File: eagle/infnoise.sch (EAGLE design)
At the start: 25 parts, among them SW1 NS5B1G385DFT2G, SW2 NS5B1G385DFT2G, U1 FT240XQ, X1 USBPCB

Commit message: minor cleanup
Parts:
- renumbered AMP1 to AMP, CMP1 to CMP
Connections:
- net AMP1OUT: now also R9.2; no longer R9.1
- net VCC33: now also R9.1; no longer R9.2
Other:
- moved on the sheet: R9
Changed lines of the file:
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@@
 <part name="R3" library="infnoise" deviceset="RESISTOR" device="0402-RES" value="10K"/>
 <part name="R4" library="infnoise" deviceset="RESISTOR" device="0402-RES" value="10K"/>
-<part name="AMP1" library="infnoise" deviceset="TSV912" device="IQ2T"/>
-<part name="CMP1" library="infnoise" deviceset="TC75W57" device="FK"/>
+<part name="AMP" library="infnoise" deviceset="TSV912" device="IQ2T"/>
+<part name="CMP" library="infnoise" deviceset="TC75W57" device="FK"/>
 <part name="SUPPLY1" library="supply2" deviceset="GND" device=""/>
 <part name="R9" library="infnoise" deviceset="RESISTOR" device="0402-RES" value="8.2K"/>
@@
 <instance part="R3" gate="G$1" x="119.38" y="30.48" rot="R270"/>
 <instance part="R4" gate="G$1" x="119.38" y="10.16" rot="R270"/>
-<instance part="AMP1" gate="G$1" x="208.28" y="50.8"/>
-<instance part="CMP1" gate="G$1" x="208.28" y="15.24"/>
+<instance part="AMP" gate="G$1" x="208.28" y="50.8"/>
+<instance part="CMP" gate="G$1" x="208.28" y="15.24"/>
 <instance part="SUPPLY1" gate="GND" x="66.04" y="-15.24"/>
-<instance part="R9" gate="G$1" x="299.72" y="58.42" rot="R90"/>
+<instance part="R9" gate="G$1" x="299.72" y="58.42" rot="R270"/>
 <instance part="R10" gate="G$1" x="299.72" y="27.94" rot="R90"/>
 <instance part="SW1" gate="G$1" x="142.24" y="50.8"/>
@@
 <wire x1="154.94" y1="35.56" x2="154.94" y2="-10.16" width="0.1524" layer="91"/>
 <wire x1="147.32" y1="40.64" x2="147.32" y2="-10.16" width="0.1524" layer="91"/>
-<pinref part="AMP1" gate="G$1" pin="GND"/>
+<pinref part="AMP" gate="G$1" pin="GND"/>
 <wire x1="182.88" y1="45.72" x2="180.34" y2="45.72" width="0.1524" layer="91"/>
 <wire x1="180.34" y1="45.72" x2="180.34" y2="10.16" width="0.1524" layer="91"/>
-<pinref part="CMP1" gate="G$1" pin="VSS"/>
+<pinref part="CMP" gate="G$1" pin="VSS"/>
 <wire x1="180.34" y1="10.16" x2="180.34" y2="-10.16" width="0.1524" layer="91"/>
 <wire x1="182.88" y1="10.16" x2="180.34" y2="10.16" width="0.1524" layer="91"/>
@@
 <wire x1="147.32" y1="60.96" x2="147.32" y2="88.9" width="0.1524" layer="91"/>
 <wire x1="147.32" y1="88.9" x2="238.76" y2="88.9" width="0.1524" layer="91"/>
-<pinref part="CMP1" gate="G$1" pin="VDD"/>
+<pinref part="CMP" gate="G$1" pin="VDD"/>
 <wire x1="238.76" y1="88.9" x2="276.86" y2="88.9" width="0.1524" layer="91"/>
 <wire x1="276.86" y1="88.9" x2="299.72" y2="88.9" width="0.1524" layer="91"/>
 <wire x1="236.22" y1="25.4" x2="238.76" y2="25.4" width="0.1524" layer="91"/>
 <wire x1="238.76" y1="25.4" x2="238.76" y2="60.96" width="0.1524" layer="91"/>
-<pinref part="AMP1" gate="G$1" pin="VCC"/>
+<pinref part="AMP" gate="G$1" pin="VCC"/>
 <wire x1="238.76" y1="60.96" x2="238.76" y2="88.9" width="0.1524" layer="91"/>
 <wire x1="236.22" y1="60.96" x2="238.76" y2="60.96" width="0.1524" layer="91"/>
-<pinref part="R9" gate="G$1" pin="2"/>
-<wire x1="299.72" y1="63.5" x2="299.72" y2="88.9" width="0.1524" layer="91"/>
 <pinref part="SW1" gate="G$1" pin="VCC"/>
 <pinref part="SW2" gate="G$1" pin="VCC"/>
@@
 <wire x1="119.38" y1="35.56" x2="119.38" y2="88.9" width="0.1524" layer="91"/>
 <junction x="119.38" y="88.9"/>
+<pinref part="R9" gate="G$1" pin="1"/>
+<wire x1="299.72" y1="88.9" x2="299.72" y2="63.5" width="0.1524" layer="91"/>
 </segment>
 </net>
 <net name="A" class="0">
 <segment>
-<pinref part="AMP1" gate="G$1" pin="IN1+"/>
+<pinref part="AMP" gate="G$1" pin="IN1+"/>
 <wire x1="182.88" y1="50.8" x2="162.56" y2="50.8" width="0.1524" layer="91"/>
 <pinref part="C7" gate="G$1" pin="1"/>
@@
 <wire x1="154.94" y1="50.8" x2="149.86" y2="50.8" width="0.1524" layer="91"/>
 <wire x1="154.94" y1="43.18" x2="154.94" y2="50.8" width="0.1524" layer="91"/>
-<pinref part="CMP1" gate="G$1" pin="IN1+"/>
+<pinref part="CMP" gate="G$1" pin="IN1+"/>
 <wire x1="182.88" y1="15.24" x2="162.56" y2="15.24" width="0.1524" layer="91"/>
 <wire x1="162.56" y1="15.24" x2="162.56" y2="50.8" width="0.1524" layer="91"/>
@@
 <wire x1="180.34" y1="76.2" x2="292.1" y2="76.2" width="0.1524" layer="91"/>
 <pinref part="R6" gate="G$1" pin="2"/>
-<pinref part="AMP1" gate="G$1" pin="OUT1"/>
+<pinref part="AMP" gate="G$1" pin="OUT1"/>
 <wire x1="182.88" y1="60.96" x2="180.34" y2="60.96" width="0.1524" layer="91"/>
 <wire x1="180.34" y1="60.96" x2="177.8" y2="60.96" width="0.1524" layer="91"/>
 <wire x1="180.34" y1="60.96" x2="180.34" y2="76.2" width="0.1524" layer="91"/>
 <junction x="180.34" y="60.96"/>
-<pinref part="R9" gate="G$1" pin="1"/>
-<wire x1="299.72" y1="45.72" x2="299.72" y2="53.34" width="0.1524" layer="91"/>
 <pinref part="SW2" gate="G$1" pin="COM"/>
 <wire x1="289.56" y1="45.72" x2="292.1" y2="45.72" width="0.1524" layer="91"/>
-<junction x="299.72" y="45.72"/>
 <pinref part="R10" gate="G$1" pin="2"/>
 <wire x1="292.1" y1="45.72" x2="299.72" y2="45.72" width="0.1524" layer="91"/>
@@
 <wire x1="292.1" y1="76.2" x2="292.1" y2="45.72" width="0.1524" layer="91"/>
 <junction x="292.1" y="45.72"/>
+<pinref part="R9" gate="G$1" pin="2"/>
+<wire x1="299.72" y1="53.34" x2="299.72" y2="45.72" width="0.1524" layer="91"/>
 </segment>
 </net>
 <net name="FB1" class="0">
 <segment>
-<pinref part="AMP1" gate="G$1" pin="IN1-"/>
+<pinref part="AMP" gate="G$1" pin="IN1-"/>
 <wire x1="182.88" y1="55.88" x2="167.64" y2="55.88" width="0.1524" layer="91"/>
 <wire x1="167.64" y1="55.88" x2="167.64" y2="60.96" width="0.1524" layer="91"/>
@@
 <wire x1="132.08" y1="50.8" x2="134.62" y2="50.8" width="0.1524" layer="91"/>
 <pinref part="SW1" gate="G$1" pin="COM"/>
-<pinref part="AMP1" gate="G$1" pin="OUT2"/>
+<pinref part="AMP" gate="G$1" pin="OUT2"/>
 <pinref part="R7" gate="G$1" pin="1"/>
 <wire x1="246.38" y1="55.88" x2="243.84" y2="55.88" width="0.1524" layer="91"/>
@@
 <segment>
 <pinref part="R7" gate="G$1" pin="2"/>
-<pinref part="AMP1" gate="G$1" pin="IN2-"/>
+<pinref part="AMP" gate="G$1" pin="IN2-"/>
 <wire x1="236.22" y1="50.8" x2="256.54" y2="50.8" width="0.1524" layer="91"/>
 <wire x1="256.54" y1="50.8" x2="256.54" y2="55.88" width="0.1524" layer="91"/>
@@
 <net name="B" class="0">
 <segment>
-<pinref part="AMP1" gate="G$1" pin="IN2+"/>
+<pinref part="AMP" gate="G$1" pin="IN2+"/>
 <wire x1="274.32" y1="45.72" x2="269.24" y2="45.72" width="0.1524" layer="91"/>
 <wire x1="269.24" y1="45.72" x2="261.62" y2="45.72" width="0.1524" layer="91"/>
 <wire x1="261.62" y1="45.72" x2="236.22" y2="45.72" width="0.1524" layer="91"/>
-<pinref part="CMP1" gate="G$1" pin="IN2+"/>
+<pinref part="CMP" gate="G$1" pin="IN2+"/>
 <wire x1="236.22" y1="10.16" x2="261.62" y2="10.16" width="0.1524" layer="91"/>
 <wire x1="261.62" y1="10.16" x2="261.62" y2="45.72" width="0.1524" layer="91"/>
@@
 <net name="COMP1" class="0">
 <segment>
-<pinref part="CMP1" gate="G$1" pin="OUT1"/>
+<pinref part="CMP" gate="G$1" pin="OUT1"/>
 <wire x1="182.88" y1="25.4" x2="167.64" y2="25.4" width="0.1524" layer="91"/>
 <wire x1="167.64" y1="25.4" x2="132.08" y2="25.4" width="0.1524" layer="91"/>
@@
 <net name="COMP2" class="0">
 <segment>
-<pinref part="CMP1" gate="G$1" pin="OUT2"/>
+<pinref part="CMP" gate="G$1" pin="OUT2"/>
 <wire x1="236.22" y1="20.32" x2="256.54" y2="20.32" width="0.1524" layer="91"/>
 <wire x1="256.54" y1="20.32" x2="256.54" y2="-5.08" width="0.1524" layer="91"/>
@@
 <net name="VREF" class="0">
 <segment>
-<pinref part="CMP1" gate="G$1" pin="IN1-"/>
+<pinref part="CMP" gate="G$1" pin="IN1-"/>
 <wire x1="182.88" y1="20.32" x2="160.02" y2="20.32" width="0.1524" layer="91"/>
 <wire x1="160.02" y1="20.32" x2="160.02" y2="0" width="0.1524" layer="91"/>
 <wire x1="160.02" y1="0" x2="238.76" y2="0" width="0.1524" layer="91"/>
 <wire x1="238.76" y1="0" x2="238.76" y2="15.24" width="0.1524" layer="91"/>
-<pinref part="CMP1" gate="G$1" pin="IN2-"/>
+<pinref part="CMP" gate="G$1" pin="IN2-"/>
 <wire x1="238.76" y1="15.24" x2="236.22" y2="15.24" width="0.1524" layer="91"/>
 <wire x1="160.02" y1="20.32" x2="119.38" y2="20.32" width="0.1524" layer="91"/>

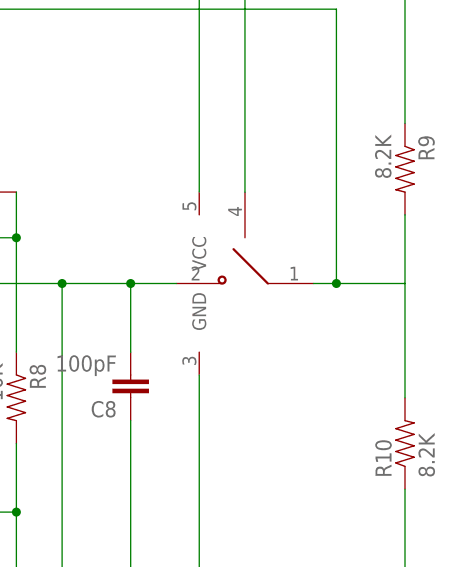
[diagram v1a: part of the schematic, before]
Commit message: Increased widths and spacing based on advice on web
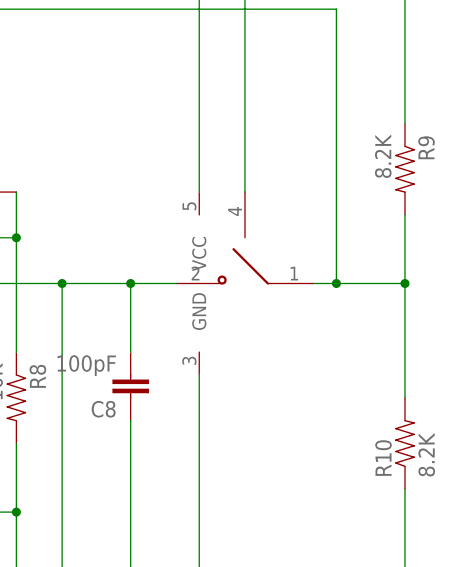
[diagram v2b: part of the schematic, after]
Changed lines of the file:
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@@
 <pinref part="R9" gate="G$1" pin="2"/>
 <wire x1="299.72" y1="53.34" x2="299.72" y2="45.72" width="0.1524" layer="91"/>
+<junction x="299.72" y="45.72"/>
 </segment>
 </net>

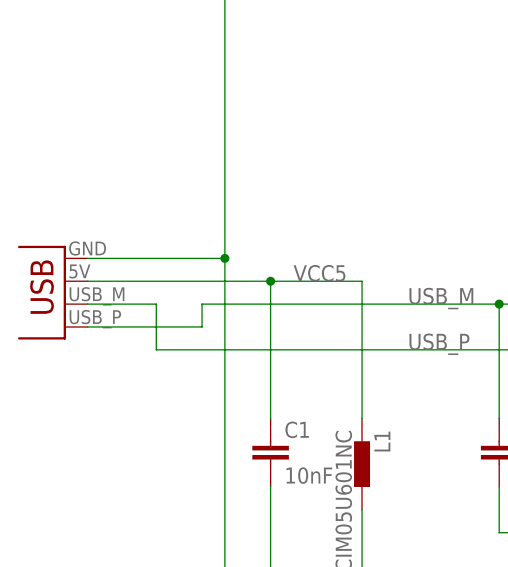
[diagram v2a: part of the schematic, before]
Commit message: Changed to real USB connector
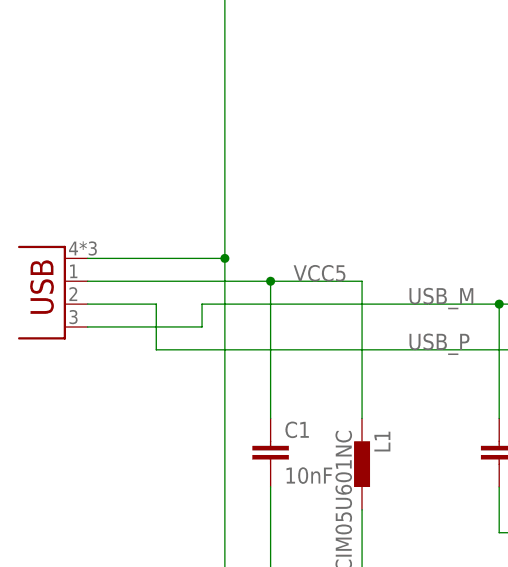
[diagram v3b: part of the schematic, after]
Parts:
- X1: value USBPCB -> USBCON; device infnoise:USBPCB -> infnoise:USBCON
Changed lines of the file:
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@@
 <parts>
 <part name="U1" library="infnoise" deviceset="FT240X" device="Q"/>
-<part name="X1" library="infnoise" deviceset="USB" device="PCB"/>
 <part name="C4" library="infnoise" deviceset="CAP" device="0402-CAP" value="47pF"/>
 <part name="C5" library="infnoise" deviceset="CAP" device="0402-CAP" value="47pF"/>
@@
 <part name="SW1" library="infnoise" deviceset="NS5B1G385" device="DFT2G"/>
 <part name="SW2" library="infnoise" deviceset="NS5B1G385" device="DFT2G"/>
+<part name="X1" library="infnoise" deviceset="USB" device="CON"/>
 </parts>
 <sheets>
@@
 <instances>
 <instance part="U1" gate="G$1" x="66.04" y="38.1" rot="R270"/>
-<instance part="X1" gate="G$1" x="-43.18" y="40.64" rot="R180"/>
 <instance part="C4" gate="G$1" x="5.08" y="17.78"/>
 <instance part="C5" gate="G$1" x="15.24" y="17.78"/>
@@
 <instance part="SW1" gate="G$1" x="142.24" y="50.8"/>
 <instance part="SW2" gate="G$1" x="281.94" y="45.72" rot="MR0"/>
+<instance part="X1" gate="G$1" x="-43.18" y="40.64" rot="R180"/>
 </instances>
 <busses>
@@
 <wire x1="5.08" y1="35.56" x2="-27.94" y2="35.56" width="0.1524" layer="91"/>
 <wire x1="-27.94" y1="35.56" x2="-27.94" y2="33.02" width="0.1524" layer="91"/>
-<pinref part="X1" gate="G$1" pin="D+"/>
 <wire x1="-27.94" y1="33.02" x2="-40.64" y2="33.02" width="0.1524" layer="91"/>
 <pinref part="C4" gate="G$1" pin="1"/>
@@
 <label x="-5.08" y="35.56" size="1.778" layer="95"/>
 <junction x="5.08" y="35.56"/>
+<pinref part="X1" gate="G$1" pin="D+"/>
 </segment>
 </net>
@@
 <wire x1="15.24" y1="30.48" x2="-33.02" y2="30.48" width="0.1524" layer="91"/>
 <wire x1="-33.02" y1="30.48" x2="-33.02" y2="35.56" width="0.1524" layer="91"/>
-<pinref part="X1" gate="G$1" pin="D-"/>
 <wire x1="-33.02" y1="35.56" x2="-40.64" y2="35.56" width="0.1524" layer="91"/>
 <pinref part="C5" gate="G$1" pin="1"/>
@@
 <label x="-5.08" y="30.48" size="1.778" layer="95"/>
 <junction x="15.24" y="30.48"/>
+<pinref part="X1" gate="G$1" pin="D-"/>
 </segment>
 </net>
 <net name="VCC5" class="0">
 <segment>
-<pinref part="X1" gate="G$1" pin="VBUS"/>
 <wire x1="-40.64" y1="38.1" x2="-20.32" y2="38.1" width="0.1524" layer="91"/>
 <wire x1="-20.32" y1="38.1" x2="-10.16" y2="38.1" width="0.1524" layer="91"/>
@@
 <pinref part="L1" gate="G$1" pin="1"/>
 <wire x1="-10.16" y1="22.86" x2="-10.16" y2="38.1" width="0.1524" layer="91"/>
+<pinref part="X1" gate="G$1" pin="VBUS"/>
 </segment>
 </net>
@@
 <pinref part="SUPPLY1" gate="GND" pin="GND"/>
 <wire x1="66.04" y1="-12.7" x2="66.04" y2="-10.16" width="0.1524" layer="91"/>
-<pinref part="X1" gate="G$1" pin="GND"/>
 <wire x1="-40.64" y1="40.64" x2="-25.4" y2="40.64" width="0.1524" layer="91"/>
 <wire x1="-25.4" y1="40.64" x2="-25.4" y2="-10.16" width="0.1524" layer="91"/>
@@
 <wire x1="119.38" y1="5.08" x2="119.38" y2="-10.16" width="0.1524" layer="91"/>
 <junction x="119.38" y="-10.16"/>
-</segment>
-</net>
+<pinref part="X1" gate="G$1" pin="GND"/>
+</segment>
+</net>

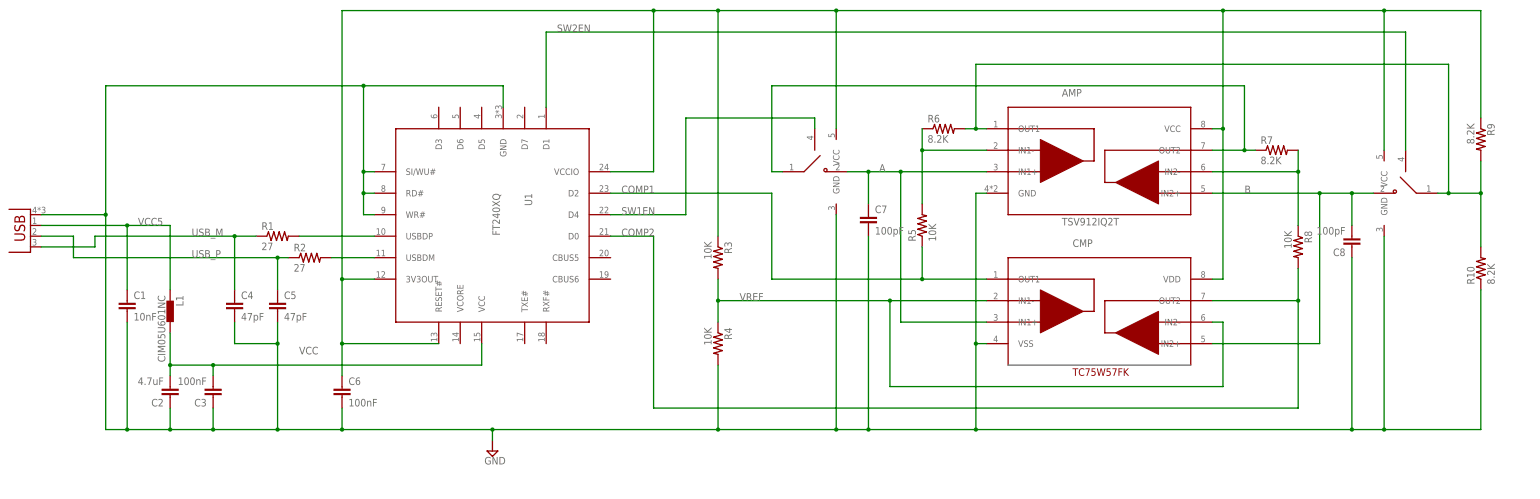
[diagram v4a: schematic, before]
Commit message: Modified board to fit USB stick enclosure
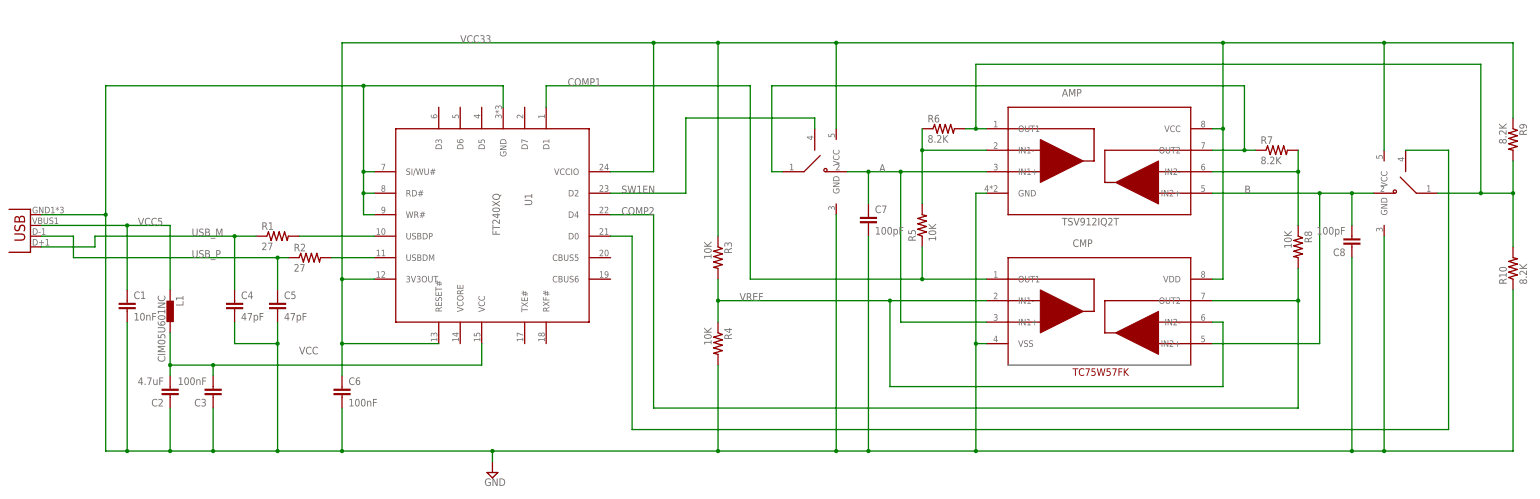
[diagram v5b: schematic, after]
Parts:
- X1: value USBCON -> USBSMT-MALE; device infnoise:USBCON -> infnoise:USBSMT-MALE
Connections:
- removed net SW2EN: SW2.IN, U1.D1
- new net N$1: SW2.IN, U1.D0
- net COMP1: now also U1.D1; no longer U1.D2
- net COMP2: now also U1.D4; no longer U1.D0
- net SW1EN: now also U1.D2; no longer U1.D4
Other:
- moved on the sheet: R10, R9
